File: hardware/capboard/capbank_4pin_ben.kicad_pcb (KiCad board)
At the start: 2 copper layers, 100 x 40 mm, 31 parts, among them SW1 SW_Push_1TS009xxxx-xxxx-xxxx_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, U1 HT7550-1, U2 MT3608

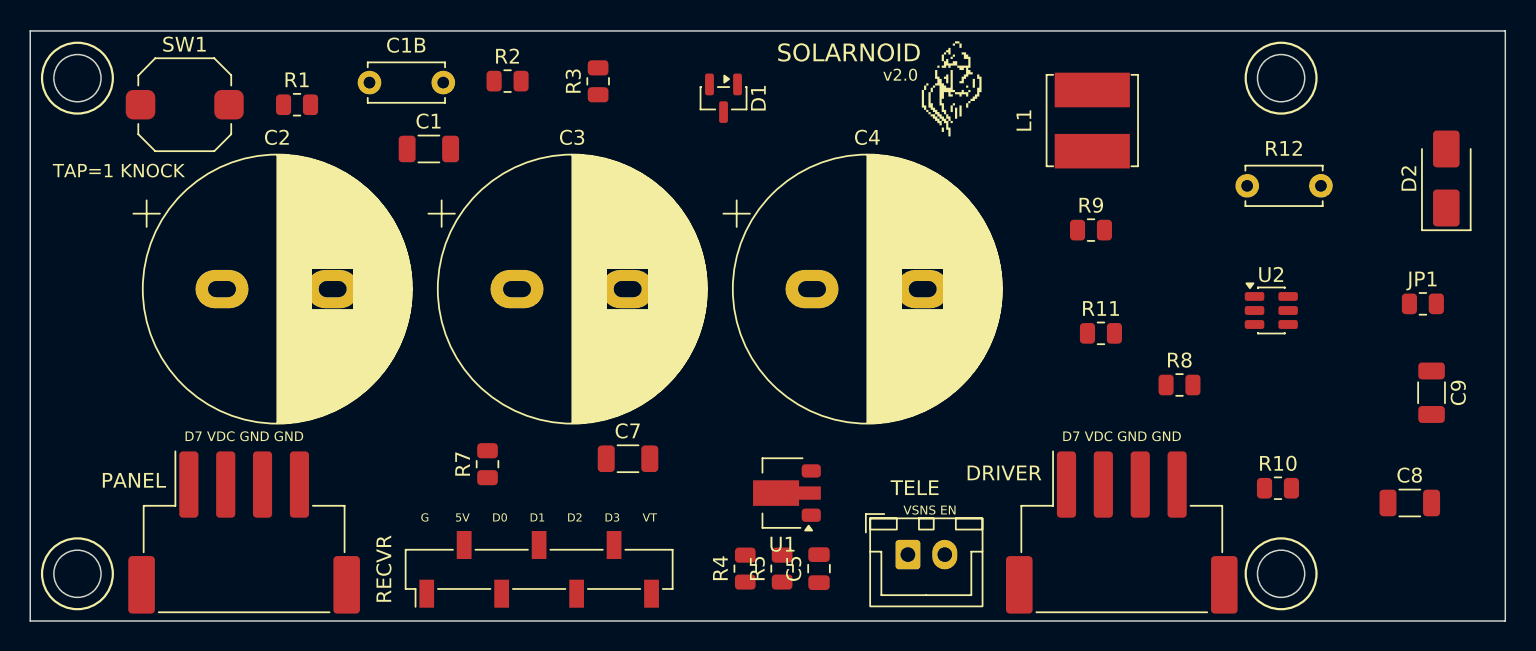
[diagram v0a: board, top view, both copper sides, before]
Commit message: hardware/capboard: fold Ben's 4pin edits into the placement (PANEL +1mm, TELE -0.5mm, v2.0); re-export
He edited the ROUTED board directly, which route_4pin.py would have overwritten.
Backed it up as capbank_4pin_ben.kicad_pcb, synced positions + silk into
capbank_placement_4pin.kicad_pcb, and re-ran the router: regenerated board
matches his footprint positions and silk exactly, DRC clean, and the router
covers natively what he had hand-patched with 5 extra tracks (161 -> 156).

Co-Authored-By: Claude Fable 5 <noreply@anthropic.com>
Claude-Session: https://claude.ai/code/session_01XEHUfVFPdvg3k1kXt9D9MK
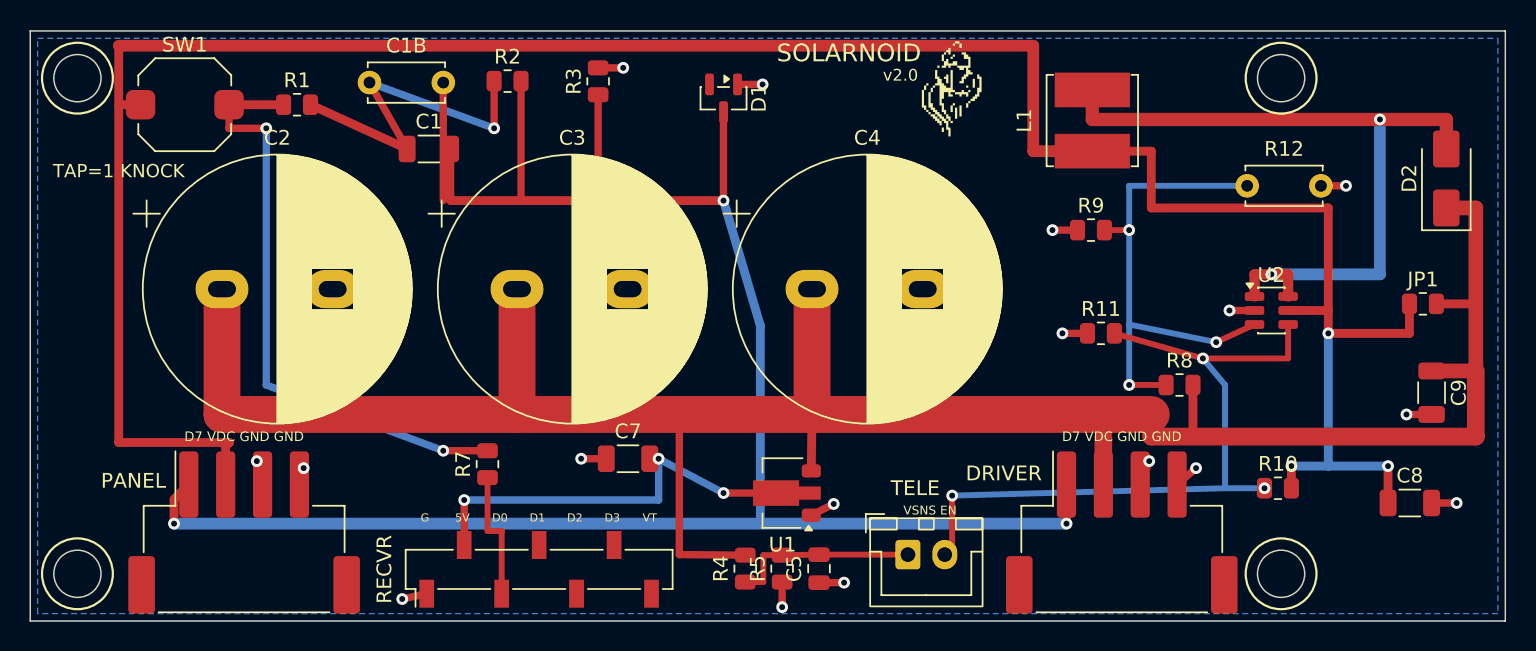
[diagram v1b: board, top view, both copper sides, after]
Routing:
- net VDCIN: track 0.00 -> 170.1 mm, vias 0 -> 3
- net VBOOST: track 0.00 -> 159.7 mm
- net D7: track 0.00 -> 139.7 mm, vias 0 -> 3
- net SW: track 0.00 -> 51.1 mm, vias 0 -> 2
- net EN: track 0.00 -> 49.0 mm, vias 0 -> 3
- net NETA: track 0.00 -> 41.0 mm, vias 0 -> 2
- net FB: track 0.00 -> 34.6 mm, vias 0 -> 3
- net GND: track 0.00 -> 33.6 mm, vias 0 -> 20
- net P5V: track 0.00 -> 30.5 mm, vias 0 -> 3
- net NETB: track 0.00 -> 24.6 mm, vias 0 -> 1
- net VSNS: track 0.00 -> 13.4 mm
- net BTNP: track 0.00 -> 8.83 mm
- added copper zone on B.Cu, net GND
